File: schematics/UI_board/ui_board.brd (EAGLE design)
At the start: 100 x 80 mm, 114 parts, among them IC1 74HCT00N, IC10 74HCT32N, IC11 74HCT14N, IC12 74HCT14N, IC13 74HCT393N, IC2 74HCT151N, IC3 74HCT32N, IC4 74HCT74N, IC5 74HCT04N, IC6 74HCT32N, IC8 74HCT373N, IC9 74HCT32N

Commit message: fix ui_bord. seems to work
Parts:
- removed IC1: 74HCT00N, 74xx-eu:DIL14
- added C24: 1µF, rcl:C025-024X044
- added IC7: 74HCT14N, 74xx-eu:DIL14
- added R27: 22k, rcl:R1206
- IC5: value 74HCT04N -> 74HCT08N
- R2: value (none) -> 10k
- moved IC5 79.1 mm to (92.7, 11.4), turned to 270 degrees
- turned S14 to 270 degrees
- renumbered R1 to R2, S1 to S14
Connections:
- new net N$3: R2.1, R27.1, S14.1, S14.2
- new net N$56: C24.1, IC7.9, R27.2
- new net N$67: IC7.4
- new net N$68: IC5.10, IC7.12
- new net N$77: IC7.3
- new net N$78: IC5.8, IC8.11
- new net N$79: IC7.11
- net CHANGE_CLOCK_SELECT: now also IC5.9, IC7.1; no longer IC1.13, IC4.2, IC8.11
- net GND: now also C24.2, IC7.7; no longer IC1.7, IC10.1, IC10.2, IC5.11, IC5.3, IC5.5, IC5.9
- net N$1: now also IC5.4; no longer IC1.4
- net N$10: now also IC4.2, IC5.13, IC7.2, IC7.5; no longer IC4.12, IC5.12
- net N$2: now also IC7.10; no longer IC1.2, IC1.8
- net N$4: now also IC4.12, IC5.11; no longer IC1.11, IC5.13
- net N$5: now also IC2.6, IC4.11, IC4.3; no longer IC1.1, IC1.10, R2.1, S14.1, S14.2
- net N$8: now also IC5.12; no longer IC1.12
- net N$9: now also IC7.13, IC7.6; no longer IC4.11, IC4.3, IC5.2
- net RING_CNTR_CLOCK: now also IC5.6; no longer IC1.6
- net SELECTED_CLOCK: now also IC5.5; no longer IC1.5, IC5.1
- net SINGLE_STEP_CLOCK: now also IC7.8; no longer IC1.3, IC1.9
- net VCC: now also IC7.14; no longer IC1.14

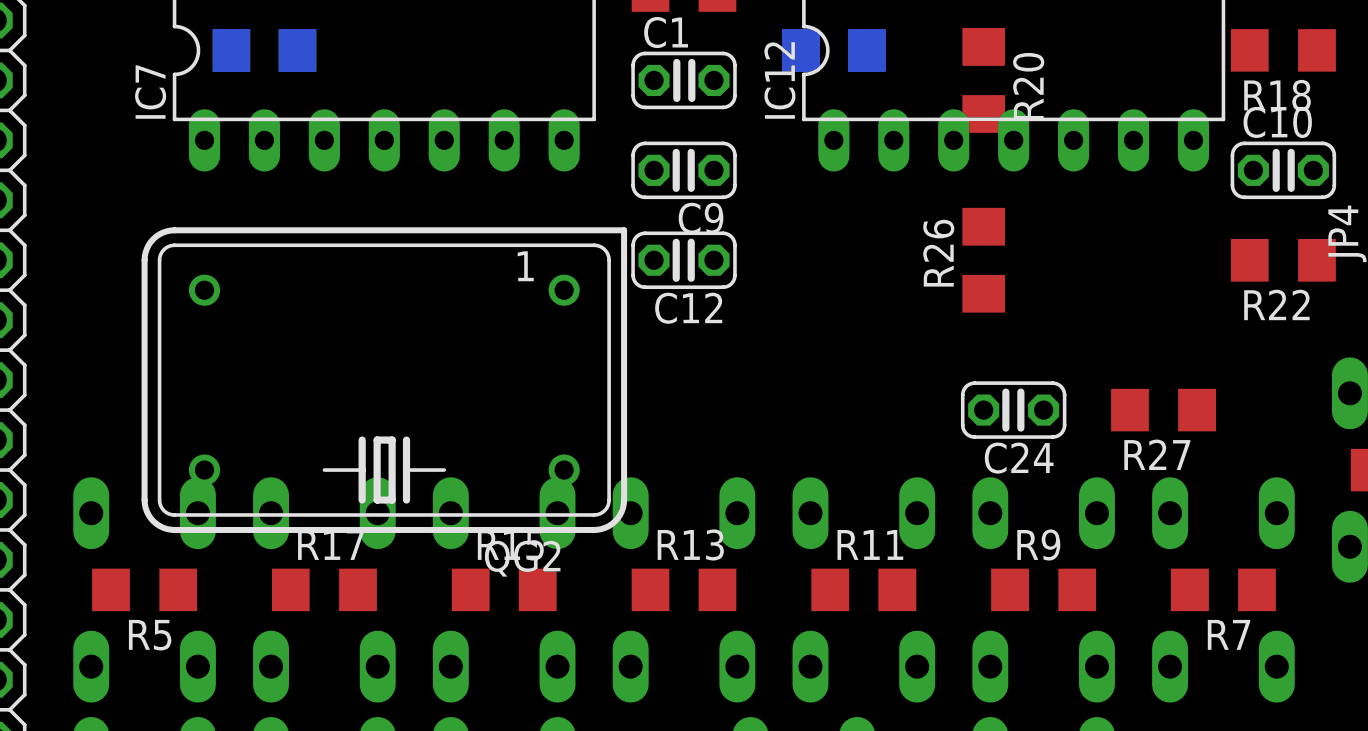
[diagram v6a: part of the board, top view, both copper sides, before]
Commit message: finished and tested ui-board.
I Didnt check all clocks. 16Mhz, 4Mhz and the single_clock work
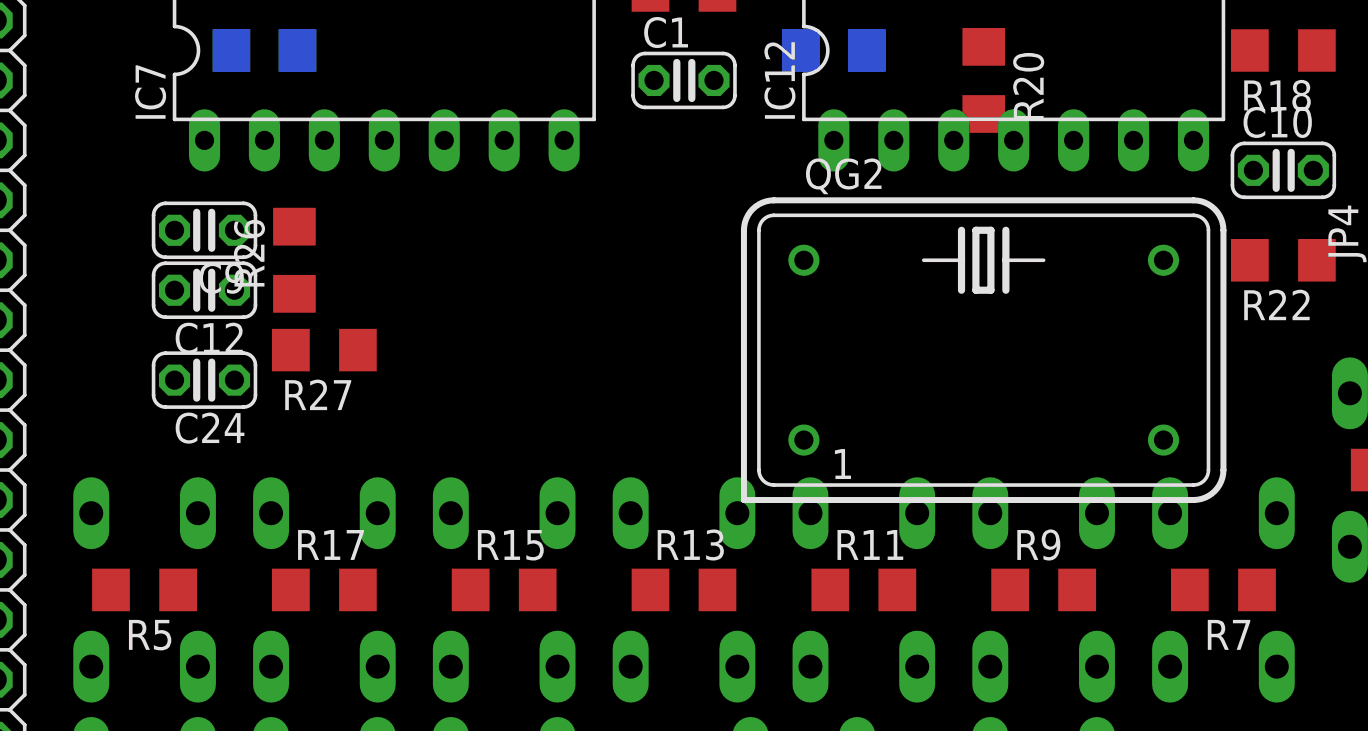
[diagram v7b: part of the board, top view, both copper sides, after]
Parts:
- moved R27 35.7 mm to (20.3, 38.1)
- moved C24 34.3 mm to (15.2, 36.8)
- moved R26 29.2 mm to (19.1, 41.9)
- moved QG2 25.4 mm to (48.3, 38.1), turned to 0 degrees
- moved C9 20.5 mm to (15.2, 43.2)
- moved C12 20.4 mm to (15.2, 40.6)
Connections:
- net 31.25KHZ renamed 250KHZ
- removed net 500KHZ: IC13.13, IC13.6, IC2.2, JP4.7
- removed net N$2: IC7.10
- removed net N$67: IC7.4
- removed net N$77: IC7.3
- removed net N$79: IC7.11
- new net 16MHZ: IC13.1, IC2.13, QG2.8
- net 1MHZ: now also IC13.13, IC13.6, IC2.2, JP4.7; no longer IC13.5, IC2.1, JP4.5
- net 2MHZ: now also IC13.5, IC2.1, JP4.5; no longer IC13.4, IC2.15, JP4.3
- net 4MHZ: now also IC13.4, IC2.15, JP4.3; no longer IC13.3, IC2.14, JP4.1
- net 8MHZ: now also IC13.3, IC2.14, JP4.1; no longer IC13.1, IC2.13, QG2.8
